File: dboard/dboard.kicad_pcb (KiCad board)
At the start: 2 copper layers, 49 x 11 mm, 10 parts, among them J1 Conn_01x04, U1 SRV05-4

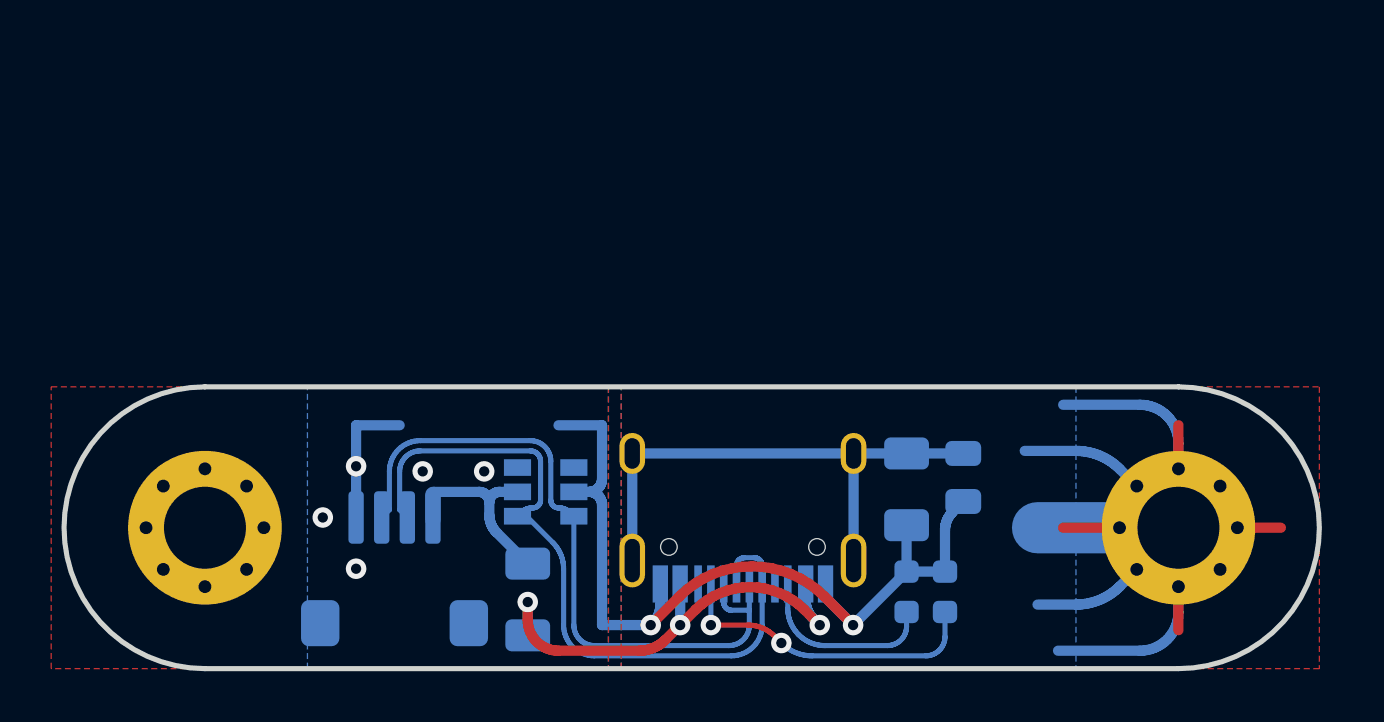
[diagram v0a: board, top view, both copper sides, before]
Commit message: Change USB footprint and make ai03 udb standard
- USB footprint was changed to use GCT USB-4085
- originally, not ai03 universal daughterboard compatible, switched
  data lines around to make this compatible
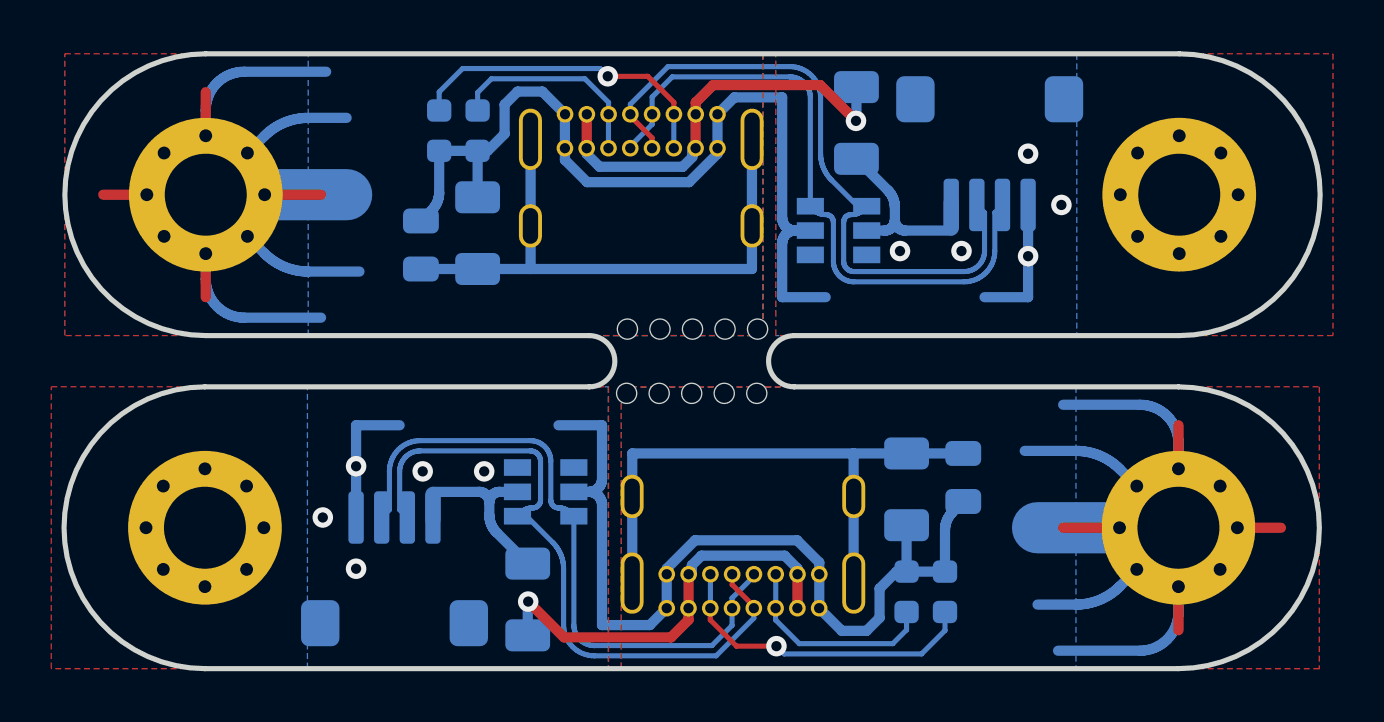
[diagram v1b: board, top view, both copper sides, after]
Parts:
- added C2: 470n, Capacitor_SMD:C_0805_2012Metric, B.Cu at (-12.6, -5.54)
- added F2: 500mA, Fuse:Fuse_1206_3216Metric, B.Cu at (4.43, -10.3)
- added H3: MountingHole_Pad, crokto:M3_Via_Hole, F.Cu at (-21.0, -7.50)
- added H4: MountingHole, crokto:M3_Via_Hole_NC, F.Cu at (17.0, -7.50)
- added J2: JST_SH_SM04B-SRSS-TB_1x04, crokto:JST_SH_SM04B-SRSS-TB_1x04-1MP_P1.00mm_Horizontal, B.Cu at (9.63, -9.35)
- added MB1: MouseBites, random-keyboard-parts:breakaway-mousebites, F.Cu at (-2.00, 0.00)
- added MB2: MouseBites, random-keyboard-parts:breakaway-mousebites, F.Cu at (-1.97, -2.00)
- added R4: 5.1K, Resistor_SMD:R_0603_1608Metric, B.Cu at (-11.9, -10.0)
- added R5: 5.1K, Resistor_SMD:R_0603_1608Metric, B.Cu at (-10.4, -10.0)
- added R6: 1M, Resistor_SMD:R_1206_3216Metric, B.Cu at (-10.4, -6.00)
- added U2: SRV05-4, Package_TO_SOT_SMD:SOT-23-6, B.Cu at (3.73, -6.10)
- added USB2: USB_C_Receptacle_USB2.0, Type-C:USB_C_GCT_USB4085, B.Cu at (-3.97, -4.54)
- J1: value Conn_01x04 -> JST_SH_SM04B-SRSS-TB_1x04
- USB1: value HRO-TYPE-C-31-M-12 -> USB_C_Receptacle_USB2.0; footprint Type-C:HRO-TYPE-C-31-M-12-Assembly -> Type-C:USB_C_GCT_USB4085
- moved USB1 2.54 mm to (0.00, 2.54)
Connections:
- J1 pad 2: D+ -> D-
- J1 pad 3: D- -> D+
- U1 pad 1: (no net) -> Net-(U1-Pad1)
- U1 pad 3: D- -> D+
- U1 pad 4: D+ -> D-
- U1 pad 6: (no net) -> Net-(U1-Pad6)
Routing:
- net SHIELD: track 74.6 -> 149.1 mm
- net GND: track 40.3 -> 81.2 mm, vias 7 -> 10
- net D-: track 27.6 -> 53.5 mm
- net D+: track 29.5 -> 51.3 mm
- net VBUS: track 18.8 -> 33.4 mm, vias 3 -> 2
- net Net-(R4-Pad2): track 0.00 -> 12.6 mm, vias 0 -> 1
- net Net-(R5-Pad2): track 0.00 -> 8.21 mm
- net +5V: track 7.74 -> 15.5 mm
- net Net-(R2-Pad2): track 7.41 -> 8.21 mm
- net Net-(R1-Pad2): track 12.5 -> 12.6 mm, vias 2 -> 1
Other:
- board size 49 x 11 mm -> 49 x 24 mm
